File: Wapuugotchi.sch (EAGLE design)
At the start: 14 parts, among them IC1 MCP170350MB, SW1 BTN B, SW2 BTN C, SW3 BTN A

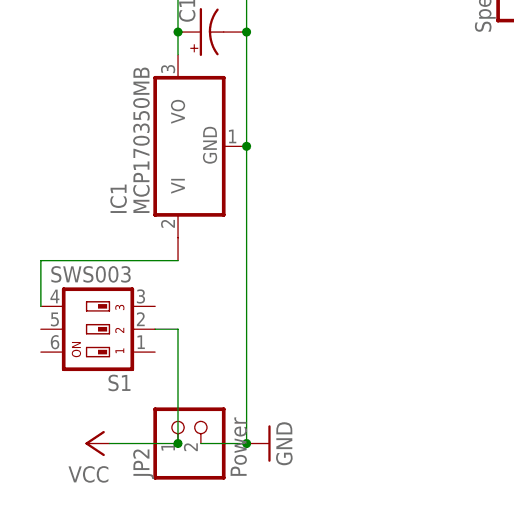
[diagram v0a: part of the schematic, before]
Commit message: Tweak the hardware to account for how the switch is wired (left side isolated from right)
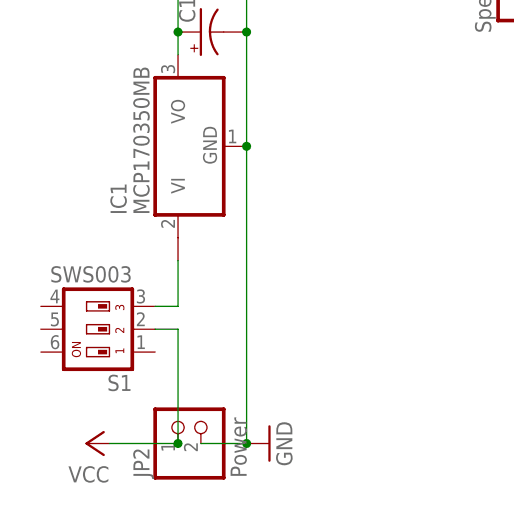
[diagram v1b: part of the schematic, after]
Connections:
- net N$12: now also S1.3; no longer S1.4
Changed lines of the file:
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@@
 <segment>
 <pinref part="IC1" gate="G$1" pin="VI1"/>
-<pinref part="S1" gate="G$1" pin="4"/>
-<wire x1="15.24" y1="60.96" x2="0" y2="60.96" width="0.1524" layer="91"/>
-<wire x1="0" y1="60.96" x2="0" y2="55.88" width="0.1524" layer="91"/>
+<pinref part="S1" gate="G$1" pin="3"/>
+<wire x1="15.24" y1="60.96" x2="15.24" y2="55.88" width="0.1524" layer="91"/>
+<wire x1="15.24" y1="55.88" x2="12.7" y2="55.88" width="0.1524" layer="91"/>
 </segment>
 </net>
